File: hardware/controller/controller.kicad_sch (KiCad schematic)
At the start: 0 parts

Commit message: Initial setup of schematic for fan controller pcb
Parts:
- added C1, C2, C3: 100nF, Capacitor_SMD:C_0805_2012Metric, symbol Device:C
- added D1: D_Schottky, Diode_SMD:D_SOD-123F, symbol Device:D_Schottky
- added J1: DC_12V_IN, 54-00286:TENSILITY_54-00286, symbol 54-00286:54-00286
- added J2: HDD_POWER_OUT, TerminalBlock_Phoenix:TerminalBlock_Phoenix_MKDS-3-2-5.08_1x02_P5.08mm_Horizontal, symbol Connector:Screw_Terminal_01x02
- added J3, J4: 470531000, CONN_SD-47053-001_H10p00_MOL, symbol Molex_470531000:470531000
- added J5: Conn_01x07, symbol Connector_Generic:Conn_01x07
- added Q1, Q2: 2N3904, Package_TO_SOT_THT:TO-92_Inline, symbol Transistor_BJT:2N3904
- added R1, R2: 4.7K, Resistor_SMD:R_0805_2012Metric, symbol Device:R
- added R10, R11, R7: 10K, Resistor_SMD:R_0805_2012Metric, symbol Device:R
- added R3, R4: 100, Resistor_SMD:R_0805_2012Metric, symbol Device:R
- added R5, R8: 1K, Resistor_SMD:R_0805_2012Metric, symbol Device:R
- added R6, R9: 100K, Resistor_SMD:R_0805_2012Metric, symbol Device:R
- added RSH1: 0.2m, CSS2H_3920R_L200F:RES_3920R_L200x_BRN, symbol CSS2H_3920R_L200F:CSS2H-3920R-L200F
- added TH1, TH2: NCU18XH103F60RB, NCU18XH103F60RB:THRMC1608X95N, symbol Murata_NCU18XH103F60RB:NCU18XH103F60RB
- added U1: TSR0.5-2450, Converter_DCDC:Converter_DCDC_TRACO_TSR0.5-24xx_TSR0.5-24xxx_THT, symbol Converter_DCDC:TSR0.5-2450
- added U2: XIAO-RP2350-SMD, Seeed_Studio_XIAO_Series:XIAO-RP2350-SMD, symbol Seeed_Studio_XIAO_Series:XIAO-RP2350-SMD
- added U3: INA228, Package_SO:TSSOP-10_3x3mm_P0.5mm, symbol Sensor_Energy:INA228
- added U4: 74HC4051, symbol 74xx:74HC4051
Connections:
- new net: C2.1, R3.2, U3.10 (Vin+)
- new net: J5.3 (Pin_3), U4.1 (A4)
- new net: J5.2 (Pin_2), U4.12 (A3)
- new net: TH1.1, U4.13 (A0)
- new net: TH2.1, U4.14 (A1)
- new net: J5.1 (Pin_1), U4.15 (A2)
- new net: C3.2, U4.16 (VCC)
- new net: J5.5 (Pin_5), U4.2 (A6)
- new net: J5.6 (Pin_6), U4.4 (A7)
- new net: J5.4 (Pin_4), U4.5 (A5)
- new net: Q1.2 (B), R5.2, R6.1
- new net: J3.4, Q1.3 (C)
- new net: C2.2, R4.2, U3.9 (Vin-)
- new net: J4.4, Q2.3 (C)
- new net: D1.2 (A), U1.3 (Vout)
- new net: Q2.2 (B), R8.2, R9.1
- new net +3.3V: C1.1, C3.1, R1.2, R10.2, R11.1, R2.2, U2.12 (3V3_OUT), U3.6 (VS)
- new net +5V: D1.1 (K), U2.14 (VBUS)
- new net 12V_HDD: J2.1 (Pin_1), R4.1, RSH1.1, U3.8 (Vbus)
- new net 12V_IN: J1.A, J3.2, J4.2, R3.1, RSH1.2, U1.1 (Vin)
- new net FAN1_PWM: R5.1, U2.8 (D7)
- new net FAN1_TACH: J3.3, R7.1, U2.9 (D8)
- new net FAN2_PWM: R8.1, U2.10 (D9)
- new net FAN2_TACH: J4.3, R10.1, U2.11 (D10)
- new net GND: C1.2, J1.C, J2.2 (Pin_2), J3.1, J4.1, J5.7 (Pin_7), Q1.1 (E), Q2.1 (E), R6.2, R9.2, TH1.2, TH2.2, U1.2 (GND), U2.13 (GND), U3.1 (A1), U3.2 (A0), U3.7 (GND), U4.6 (~{E}), U4.7 (VEE), U4.8 (GND)
- new net I2C_SCL: R2.1, U2.6 (D5), U3.5 (SCL)
- new net I2C_SDA: R1.1, U2.5 (D4), U3.4 (SDA)
- new net NTC_ADC: R11.2, U2.2 (D1), U4.3 (A)
- new net NTC_SEL0: U2.3 (D2), U4.11 (S0)
- new net NTC_SEL1: U2.4 (D3), U4.10 (S1)
- new net NTC_SEL2: U2.7 (D6), U4.9 (S2)
- no-connect marks 0 -> 19

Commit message: Qualify fan connector footprint references with project library nickname
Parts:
- J3, J4: footprint CONN_SD-47053-001_H10p00_MOL -> Molex_470531000:CONN_SD-47053-001_H10p00_MOL
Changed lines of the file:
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@@
 			)
 		)
-		(property "Footprint" "CONN_SD-47053-001_H10p00_MOL"
+		(property "Footprint" "Molex_470531000:CONN_SD-47053-001_H10p00_MOL"
 			(at 87.63 147.32 0)
 			(hide yes)
@@
 			)
 		)
-		(property "Footprint" "CONN_SD-47053-001_H10p00_MOL"
+		(property "Footprint" "Molex_470531000:CONN_SD-47053-001_H10p00_MOL"
 			(at 36.83 146.05 0)
 			(hide yes)

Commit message: Assign SOIC-16 mux and JST-XH sensor connector footprints
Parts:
- J5: footprint (none) -> Connector_JST:JST_XH_B7B-XH-A_1x07_P2.50mm_Vertical
- U4: footprint (none) -> Package_SO:SOIC-16_3.9x9.9mm_P1.27mm
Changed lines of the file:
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@@
 			)
 		)
-		(property "Footprint" ""
+		(property "Footprint" "Package_SO:SOIC-16_3.9x9.9mm_P1.27mm"
 			(at 154.94 118.11 0)
 			(hide yes)
@@
 			)
 		)
-		(property "Footprint" ""
+		(property "Footprint" "Connector_JST:JST_XH_B7B-XH-A_1x07_P2.50mm_Vertical"
 			(at 175.26 113.03 0)
 			(hide yes)

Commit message: Correct imported component footprint library references
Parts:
- TH1, TH2: footprint NCU18XH103F60RB:THRMC1608X95N -> Murata_NCU18XH103F60RB:THRMC1608X95N
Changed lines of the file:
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@@
 			)
 		)
-		(property "Footprint" "NCU18XH103F60RB:THRMC1608X95N"
+		(property "Footprint" "Murata_NCU18XH103F60RB:THRMC1608X95N"
 			(at 184.15 85.09 0)
 			(hide yes)
@@
 			)
 		)
-		(property "Footprint" "NCU18XH103F60RB:THRMC1608X95N"
+		(property "Footprint" "Murata_NCU18XH103F60RB:THRMC1608X95N"
 			(at 184.15 97.79 0)
 			(hide yes)

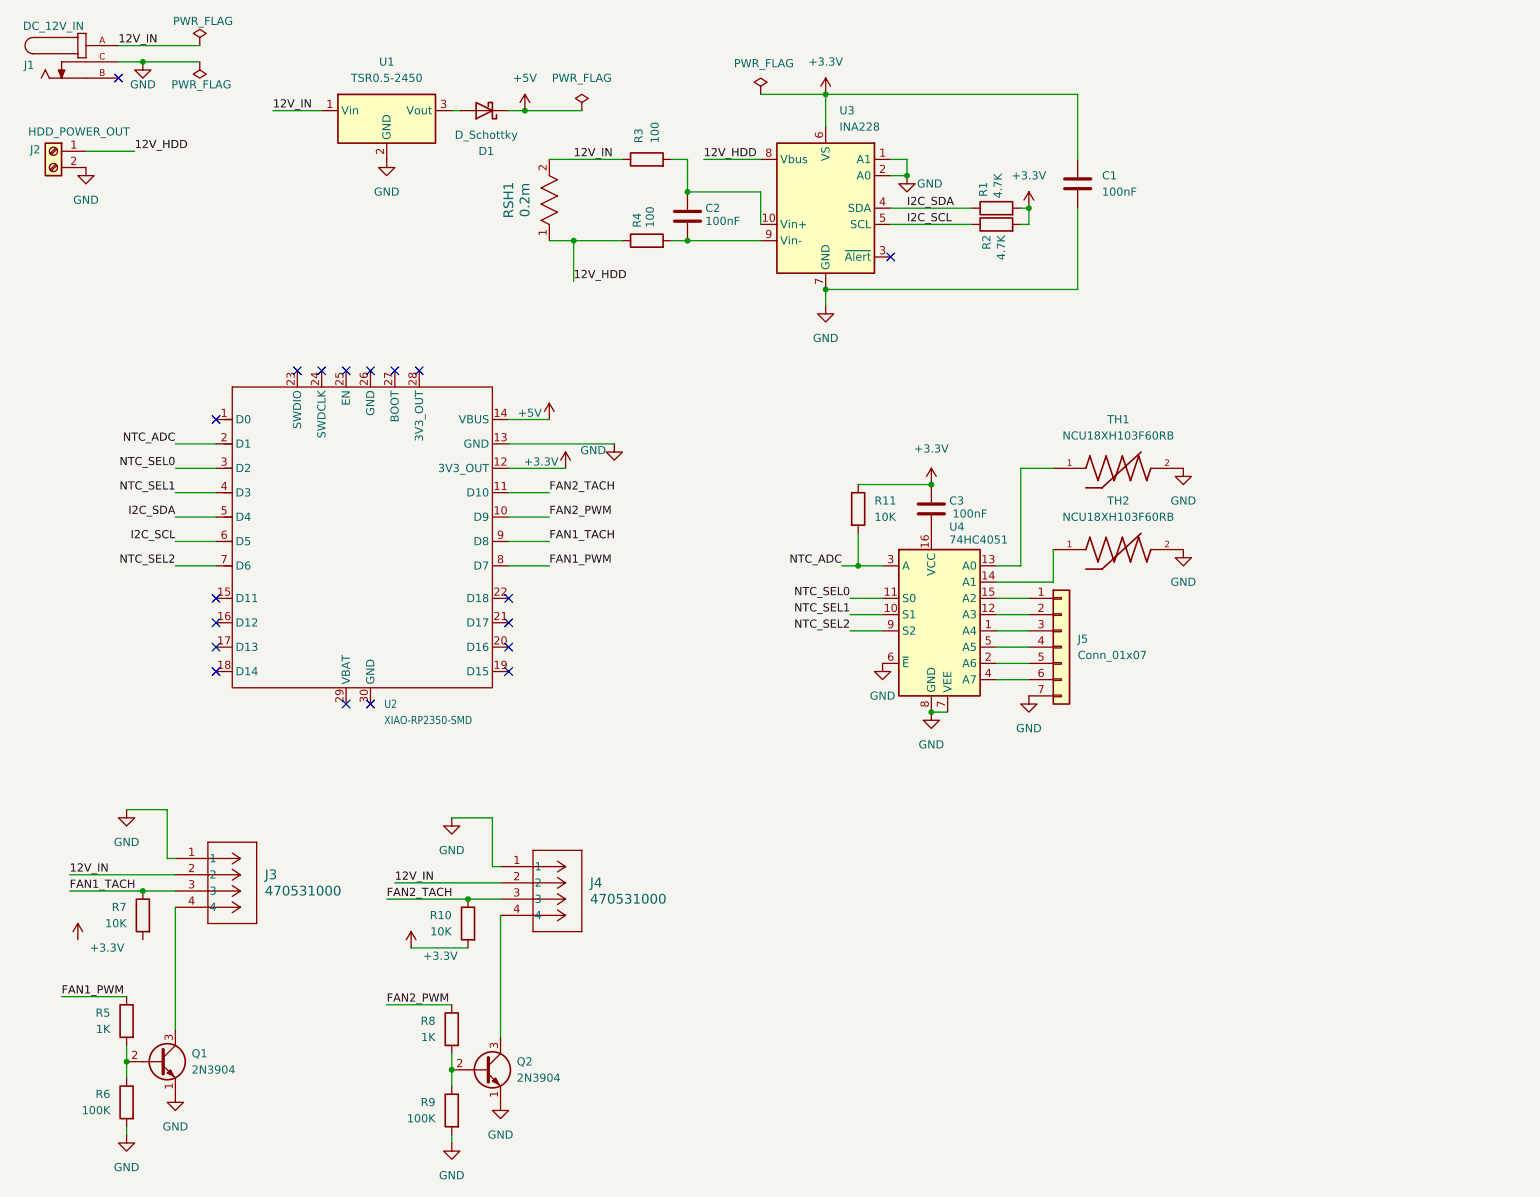
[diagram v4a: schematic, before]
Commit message: Fix C3 decoupling wiring
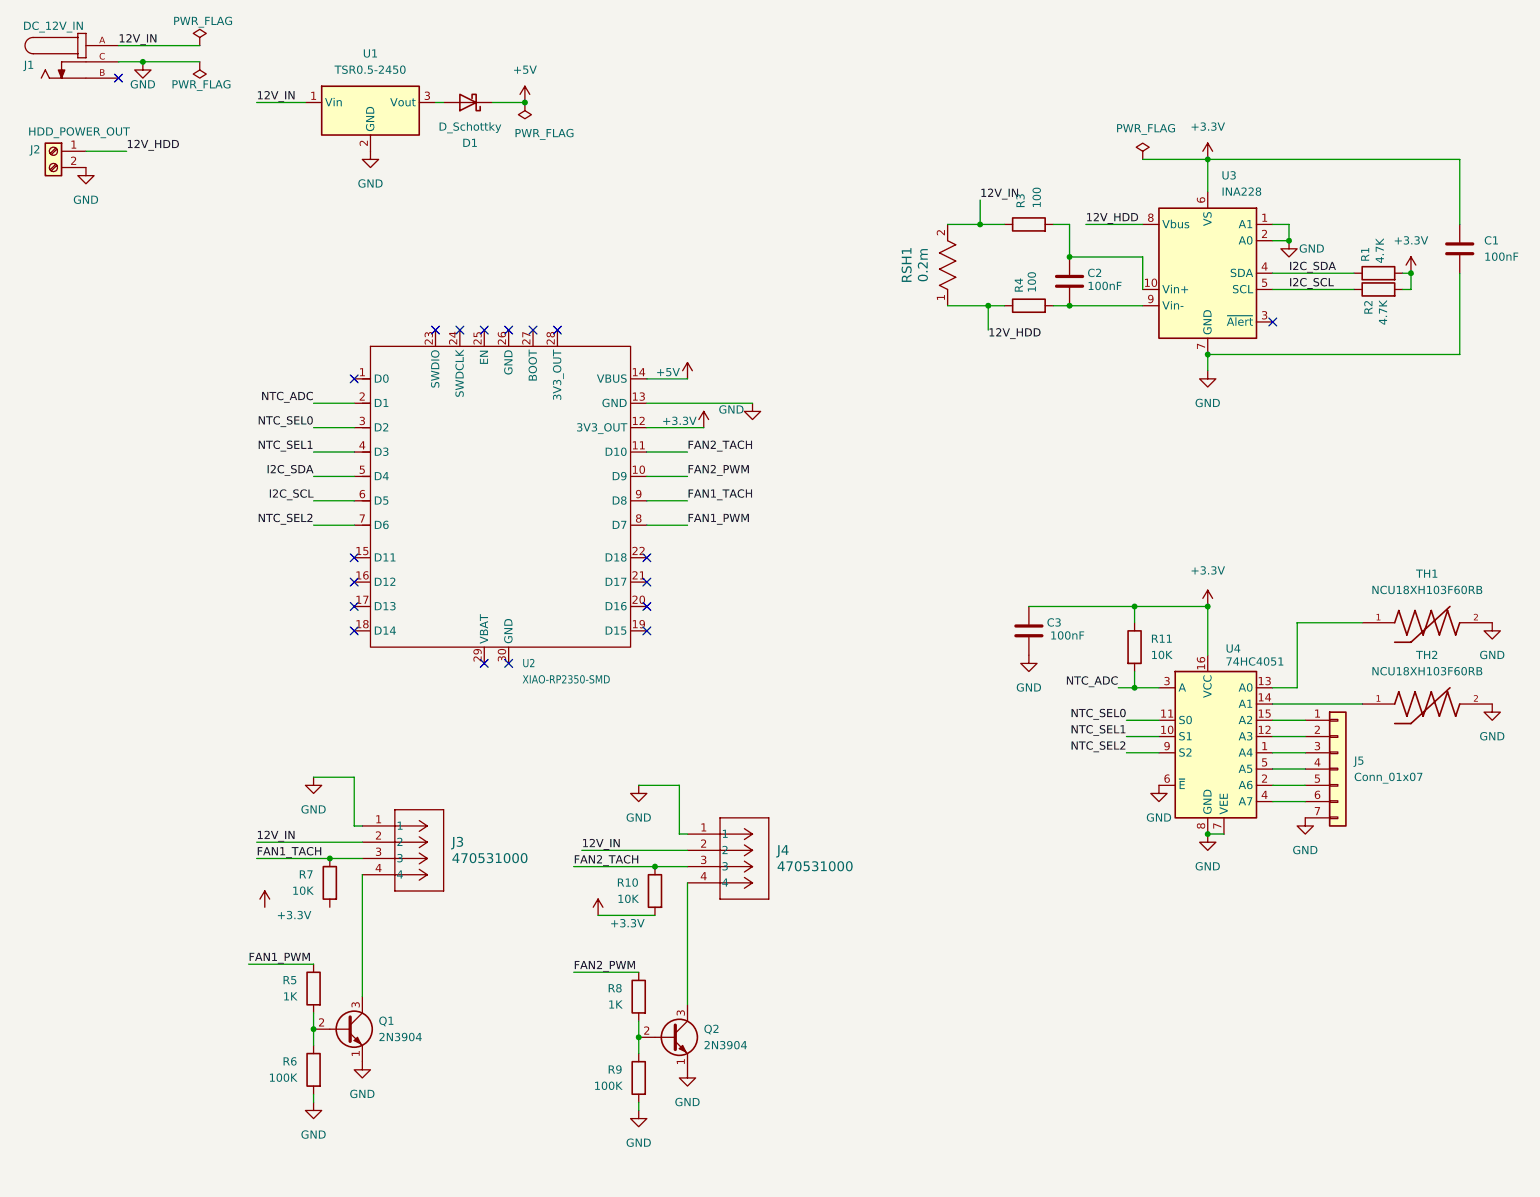
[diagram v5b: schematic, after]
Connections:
- net +3.3V: now also U4.16 (VCC)
- net GND: now also C3.2
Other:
- moved on the sheet: C1, C2, C3, D1, J3, J4, J5, Q1, Q2, R1, R10, R11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

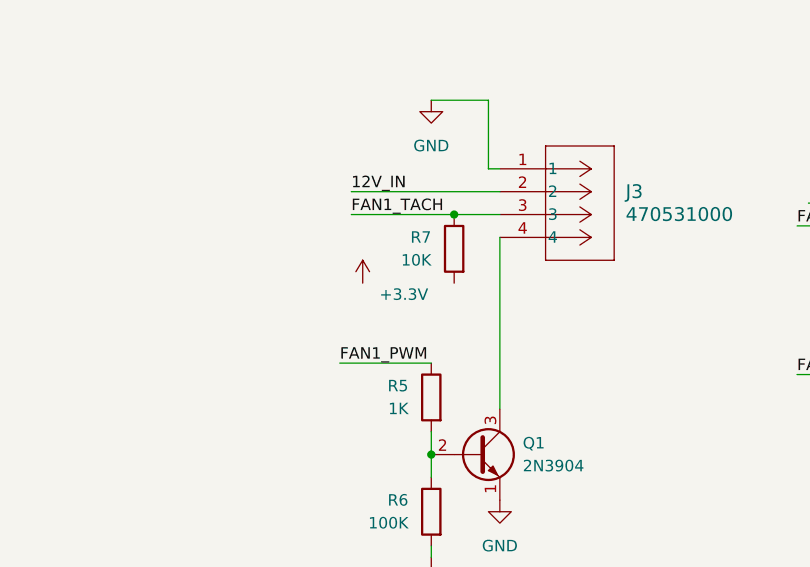
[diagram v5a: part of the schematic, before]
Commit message: Fix wiring issues found by ERC
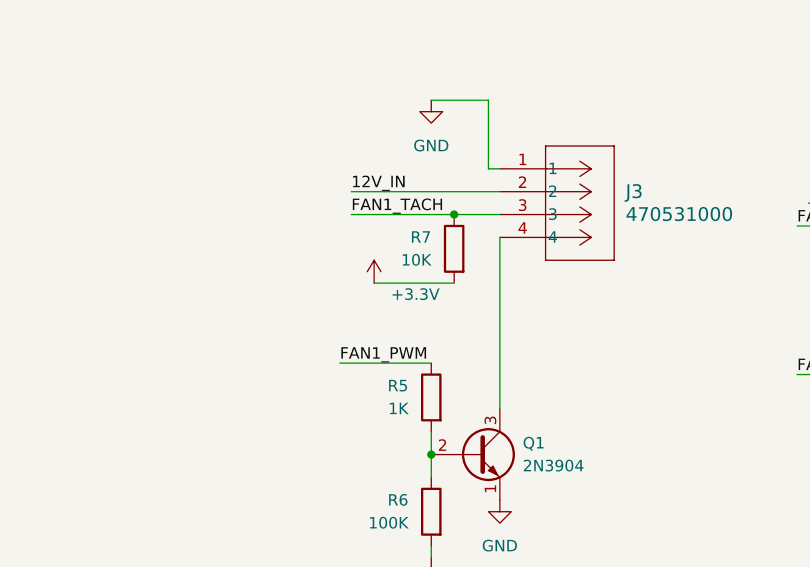
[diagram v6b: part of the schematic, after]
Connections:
- net +3.3V: now also R7.2
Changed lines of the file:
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@@
 	(wire
 		(pts
+			(xy 52.07 153.67) (xy 60.96 153.67)
+		)
+		(stroke
+			(width 0)
+			(type default)
+		)
+	)
+	(wire
+		(pts
 			(xy 208.28 57.15) (xy 220.98 57.15)
 		)
@@
 	(symbol
 		(lib_id "power:+3.3V")
-		(at 50.8 153.67 0)
+		(at 52.07 153.67 0)
 		(unit 1)
 		(body_style 1)
@@
 		(dnp no)
 		(property "Reference" "#PWR021"
-			(at 50.8 157.48 0)
+			(at 52.07 157.48 0)
 			(hide yes)
 			(show_name no)
@@
 		)
 		(property "Value" "+3.3V"
-			(at 55.372 154.94 0)
+			(at 56.642 154.94 0)
 			(show_name no)
 			(do_not_autoplace no)
@@
 		)
 		(property "Footprint" ""
-			(at 50.8 153.67 0)
+			(at 52.07 153.67 0)
 			(hide yes)
 			(show_name no)
@@
 		)
 		(property "Datasheet" ""
-			(at 50.8 153.67 0)
+			(at 52.07 153.67 0)
 			(hide yes)
 			(show_name no)
@@
 		)
 		(property "Description" "Power symbol creates a global label with name \"+3.3V\""
-			(at 50.8 153.67 0)
+			(at 52.07 153.67 0)
 			(hide yes)
 			(show_name no)
